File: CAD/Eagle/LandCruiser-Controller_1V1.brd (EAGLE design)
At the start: 98 x 63 mm, 65 parts, among them IC611 LM7805, K311 V23086C1001A403, K312 V23086C1001A403, K313 V23086C1001A403, K314 V23086C1001A403, K315 V23086C1001A403, U101 MEGA8-P, U221 SN75240, U301 MIC2981/2982SO18W, U501 MAX232_SOIC16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

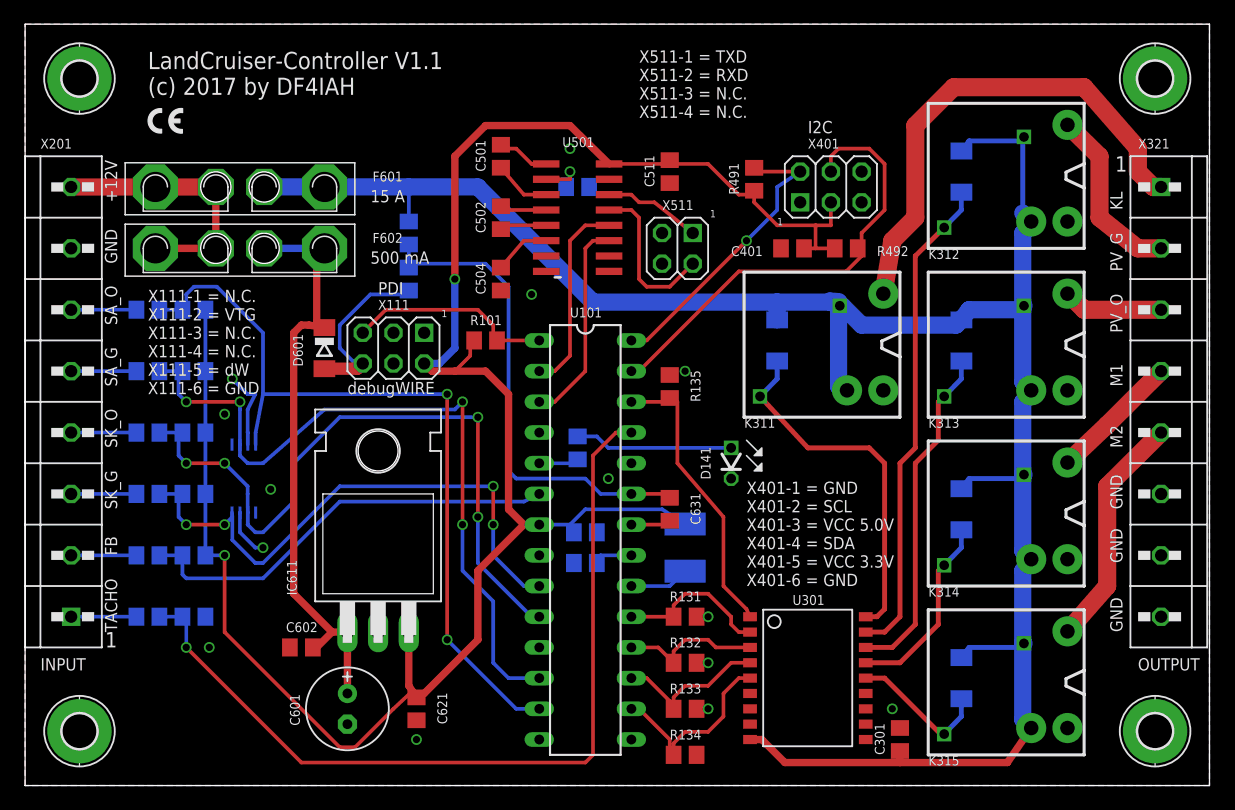
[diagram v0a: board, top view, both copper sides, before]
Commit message: HW_V1.1 - driver switches against ground, not Vbat. Another input line added.
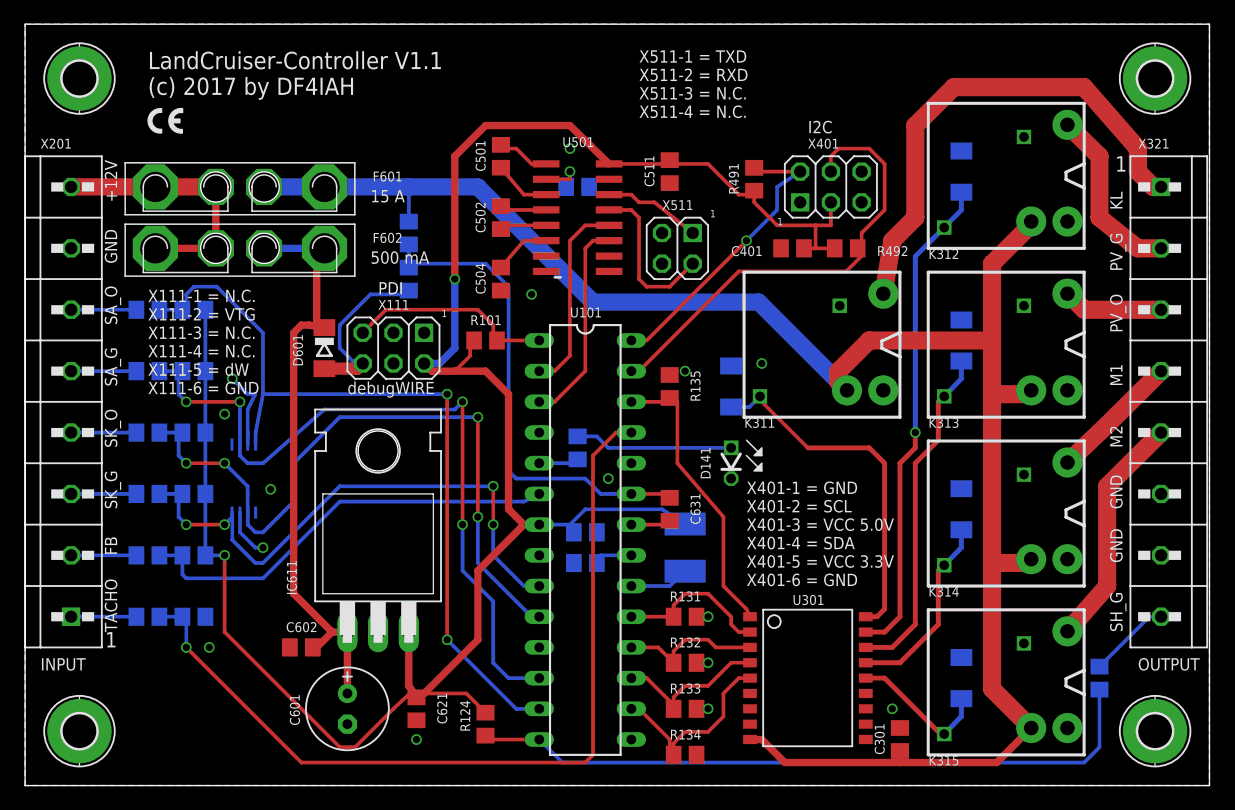
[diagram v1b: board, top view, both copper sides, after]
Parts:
- added R121: 4k7R, rcl:R0805
- added R321: 56R, rcl:R0805
- moved R124 34.1 mm to (38.1, 5.08), flipped to the top, turned to 90 degrees
- moved R122 15.2 mm to (14.0, 34.3)
- moved R123 15.2 mm to (14.0, 39.4), turned to 180 degrees
- moved R125 10.2 mm to (14.0, 24.1), turned to 0 degrees
- moved R126 10.2 mm to (14.0, 29.2), turned to 0 degrees
- moved D311 5.39 mm to (58.4, 33.0), turned to 90 degrees
- turned D312 to 90 degrees
- turned D313 to 90 degrees
- turned D314 to 90 degrees
- turned D315 to 90 degrees
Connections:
- new net MP_SH_G: R124.1, R321.1, U101.14
- new net SH_G: R321.2, X321.8
- net +12V: no longer D311.C, D312.C, D313.C, D314.C, D315.C, K311.1, K312.1, K313.1, K314.1, K315.1
- net +5V: now also R121.2, R123.2, R124.2, R125.1, R126.1; no longer R123.1, R124.1, R125.2, R126.2
- net DRV_KL: now also D311.C; no longer D311.A
- net DRV_M1: now also D314.C; no longer D314.A
- net DRV_M2: now also D315.C; no longer D315.A
- net DRV_PV_G: now also D312.C; no longer D312.A
- net DRV_PV_O: now also D313.C; no longer D313.A
- net GND: now also D311.A, D312.A, D313.A, D314.A, D315.A, K311.1, K312.1, K313.1, K314.1, K315.1; no longer X321.8
- net MP_FB: now also R121.1; no longer R122.1
- net MP_SA_G: now also R122.1; no longer R125.1
- net MP_SA_O: now also R123.1; no longer R126.1
- net MP_SK_G: now also R125.2; no longer R123.2
- net MP_SK_O: now also R126.2; no longer R124.2
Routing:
- net MP_SH_G: track 0.00 -> 57.2 mm
- net +12V: track 175.0 -> 151.2 mm
- net SH_G: track 0.00 -> 6.81 mm
- net +5V: track 173.0 -> 178.8 mm
- net GND: track 28.7 -> 29.5 mm, vias 14 -> 15
- net DRV_KL: track 30.1 -> 29.4 mm
- net DRV_PV_G: vias 0 -> 1
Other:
- board text added: "SH_G"

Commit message: HW_V1.1 - switched FB input with rear tail gate (SH_G)
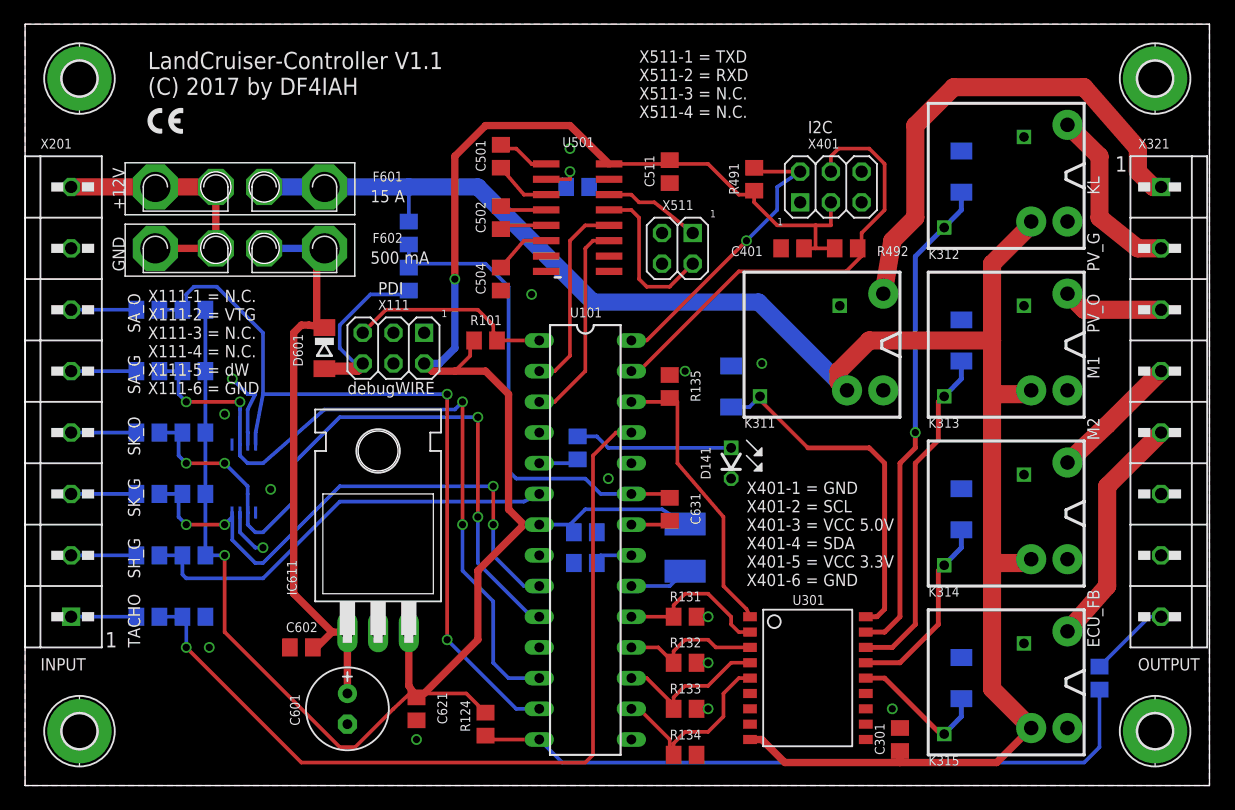
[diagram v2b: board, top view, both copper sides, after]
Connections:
- removed net ECU_FB: R212.1, X201.2
- new net ECU_FB_IN: R321.2, X321.8
- net GND: no longer U301.6, U301.7, U301.8, X321.6, X321.7
- net MP_FB: now also R124.1, R321.1, U101.14; no longer R121.1, R212.2, U101.6
- net MP_SH_G: now also R121.1, R212.2, U101.6; no longer R124.1, R321.1, U101.14
- net SH_G: now also R212.1, X201.2; no longer R321.2, X321.8
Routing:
- net MP_SH_G: track 57.2 -> 35.9 mm
- net MP_FB: track 35.9 -> 56.9 mm
- net ECU_FB_IN: track 0.00 -> 6.81 mm
- net ECU_FB: track 5.40 -> 0.00 mm
- net SH_G: track 6.81 -> 5.40 mm
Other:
- board text added: "ECU_FB"
- board text added: "LandCruiser-Controller V1.1 (C) 2017 by DF4IAH"
- board text removed: "FB"
- board text removed: "LandCruiser-Controller V1.1 (c) 2017 by DF4IAH"
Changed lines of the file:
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@@
 <layers>
 <layer number="1" name="Top" color="4" fill="1" visible="yes" active="yes"/>
-<layer number="2" name="Route2" color="1" fill="3" visible="yes" active="yes"/>
+<layer number="2" name="Route2" color="1" fill="3" visible="no" active="yes"/>
 <layer number="3" name="Route3" color="4" fill="3" visible="no" active="no"/>
 <layer number="4" name="Route4" color="1" fill="4" visible="no" active="no"/>
@@
 <dimension x1="0" y1="62.865" x2="98" y2="62.865" x3="49" y3="70.935" textsize="1.016" layer="47"/>
 <text x="10.16" y="57.15" size="1.4224" layer="21" ratio="15">LandCruiser-Controller V1.1
-(c) 2017 by DF4IAH </text>
+(C) 2017 by DF4IAH </text>
 <text x="64.77" y="53.975" size="1.016" layer="21" ratio="12">I2C</text>
 <polygon width="0.1" layer="21">
@@
 <text x="26.67" y="32.385" size="1.016" layer="21" ratio="12">debugWIRE</text>
 <text x="1.27" y="9.525" size="1.016" layer="21" ratio="12">INPUT</text>
-<text x="7.62" y="48.26" size="1.016" layer="21" ratio="12" rot="R90">+12V</text>
-<text x="7.62" y="43.18" size="1.016" layer="21" ratio="12" rot="R90">GND</text>
+<text x="8.255" y="47.625" size="1.016" layer="21" ratio="12" rot="R90">+12V</text>
+<text x="8.255" y="42.545" size="1.016" layer="21" ratio="12" rot="R90">GND</text>
 <text x="28.575" y="48.26" size="1.016" layer="21" ratio="12">15 A</text>
 <text x="28.575" y="43.18" size="1.016" layer="21" ratio="12">500 mA</text>
-<text x="7.62" y="12.7" size="1.016" layer="21" ratio="12" rot="R90">TACHO</text>
-<text x="7.62" y="19.05" size="1.016" layer="21" ratio="12" rot="R90">FB</text>
-<text x="7.62" y="22.86" size="1.016" layer="21" ratio="12" rot="R90">SK_G</text>
-<text x="7.62" y="27.94" size="1.016" layer="21" ratio="12" rot="R90">SK_O</text>
-<text x="7.62" y="33.02" size="1.016" layer="21" ratio="12" rot="R90">SA_G</text>
-<text x="7.62" y="38.1" size="1.016" layer="21" ratio="12" rot="R90">SA_O</text>
+<text x="9.525" y="11.43" size="1.016" layer="21" ratio="12" rot="R90">TACHO</text>
+<text x="9.525" y="17.145" size="1.016" layer="21" ratio="12" rot="R90">SH_G</text>
+<text x="9.525" y="22.225" size="1.016" layer="21" ratio="12" rot="R90">SK_G</text>
+<text x="9.525" y="27.305" size="1.016" layer="21" ratio="12" rot="R90">SK_O</text>
+<text x="9.525" y="32.385" size="1.016" layer="21" ratio="12" rot="R90">SA_G</text>
+<text x="9.525" y="37.465" size="1.016" layer="21" ratio="12" rot="R90">SA_O</text>
 <text x="92.075" y="9.525" size="1.016" layer="21" ratio="12">OUTPUT</text>
 <text x="50.8" y="55.245" size="1.016" layer="21" ratio="12">X511-1 = TXD
@@
 X511-3 = N.C.
 X511-4 = N.C.</text>
-<text x="90.805" y="47.625" size="1.016" layer="21" ratio="12" rot="R90">KL</text>
-<text x="90.805" y="42.545" size="1.016" layer="21" ratio="12" rot="R90">PV_G</text>
-<text x="90.805" y="37.465" size="1.016" layer="21" ratio="12" rot="R90">PV_O</text>
-<text x="90.805" y="33.02" size="1.016" layer="21" ratio="12" rot="R90">M1</text>
-<text x="90.805" y="27.94" size="1.016" layer="21" ratio="12" rot="R90">M2</text>
-<text x="90.805" y="22.86" size="1.016" layer="21" ratio="12" rot="R90">GND</text>
-<text x="90.805" y="18.415" size="1.016" layer="21" ratio="12" rot="R90">GND</text>
-<text x="90.805" y="12.7" size="1.016" layer="21" ratio="12" rot="R90">SH_G</text>
+<text x="88.9" y="48.895" size="1.016" layer="21" ratio="12" rot="R90">KL</text>
+<text x="88.9" y="42.545" size="1.016" layer="21" ratio="12" rot="R90">PV_G</text>
+<text x="88.9" y="37.465" size="1.016" layer="21" ratio="12" rot="R90">PV_O</text>
+<text x="88.9" y="33.655" size="1.016" layer="21" ratio="12" rot="R90">M1</text>
+<text x="88.9" y="28.575" size="1.016" layer="21" ratio="12" rot="R90">M2</text>
+<text x="88.9" y="11.43" size="1.016" layer="21" ratio="12" rot="R90">ECU_FB</text>
 <text x="57.15" y="47.625" size="0.6096" layer="21" ratio="20" rot="R180">1</text>
 <dimension x1="4.5" y1="4.5" x2="4.445" y2="0" x3="-1.878546875" y3="2.25" textsize="0.8128" layer="47" dtype="vertical"/>
@@
 <contactref element="IC611" pad="2"/>
 <contactref element="U301" pad="10"/>
-<contactref element="U301" pad="6"/>
-<contactref element="U301" pad="7"/>
-<contactref element="U301" pad="8"/>
 <contactref element="K314" pad="3"/>
 <contactref element="K315" pad="3"/>
-<contactref element="X321" pad="7"/>
-<contactref element="X321" pad="6"/>
 <contactref element="U501" pad="15"/>
 <contactref element="C504" pad="2"/>
@@
 </signal>
 <signal name="MP_FB">
-<contactref element="U101" pad="6"/>
-<contactref element="R212" pad="2"/>
-<contactref element="R121" pad="1"/>
-<wire x1="11.11" y1="19.05" x2="13.02" y2="19.05" width="0.3048" layer="16"/>
-<wire x1="13.02" y1="19.05" x2="13.02" y2="17.46" width="0.3048" layer="16"/>
-<wire x1="13.02" y1="17.46" x2="13.335" y2="17.145" width="0.3048" layer="16"/>
-<wire x1="13.335" y1="17.145" x2="19.685" y2="17.145" width="0.3048" layer="16"/>
-<wire x1="19.685" y1="17.145" x2="26.035" y2="23.495" width="0.3048" layer="16"/>
-<wire x1="26.035" y1="23.495" x2="41.275" y2="23.495" width="0.3048" layer="16"/>
-<wire x1="41.275" y1="23.495" x2="42.545" y2="24.13" width="0.3048" layer="16"/>
+<contactref element="R321" pad="1"/>
+<contactref element="U101" pad="14"/>
+<wire x1="42.545" y1="3.81" x2="38.1" y2="3.81" width="0.3048" layer="1"/>
+<wire x1="42.545" y1="3.81" x2="44.45" y2="1.905" width="0.3048" layer="16"/>
+<wire x1="44.45" y1="1.905" x2="87.63" y2="1.905" width="0.3048" layer="16"/>
+<wire x1="87.63" y1="1.905" x2="88.9" y2="3.175" width="0.3048" layer="16"/>
+<contactref element="R124" pad="1"/>
+<wire x1="88.9" y1="3.175" x2="88.9" y2="7.94" width="0.3048" layer="16"/>
+<wire x1="38.1" y1="4.13" x2="38.1" y2="3.81" width="0" layer="19" extent="1-1"/>
 </signal>
 <signal name="MP_SK_O">
@@
 <wire x1="69.85" y1="36.83" x2="80.01" y2="36.83" width="1.5" layer="1"/>
 </signal>
-<signal name="ECU_FB">
+<signal name="SH_G">
 <contactref element="R212" pad="1"/>
 <contactref element="X201" pad="2"/>
@@
 </signal>
 <signal name="MP_SH_G">
-<contactref element="R124" pad="1"/>
-<contactref element="U101" pad="14"/>
-<wire x1="42.545" y1="3.81" x2="38.1" y2="3.81" width="0.3048" layer="1"/>
-<wire x1="38.1" y1="3.81" x2="38.1" y2="4.13" width="0.3048" layer="1"/>
-<wire x1="42.545" y1="3.81" x2="44.45" y2="1.905" width="0.3048" layer="16"/>
-<wire x1="44.45" y1="1.905" x2="87.63" y2="1.905" width="0.3048" layer="16"/>
-<contactref element="R321" pad="1"/>
-<wire x1="87.63" y1="1.905" x2="88.9" y2="3.175" width="0.3048" layer="16"/>
-<wire x1="88.9" y1="3.175" x2="88.9" y2="7.94" width="0.3048" layer="16"/>
-</signal>
-<signal name="SH_G">
+<contactref element="R212" pad="2"/>
+<contactref element="U101" pad="6"/>
+<wire x1="13.02" y1="17.46" x2="13.335" y2="17.145" width="0.3048" layer="16"/>
+<wire x1="13.335" y1="17.145" x2="19.685" y2="17.145" width="0.3048" layer="16"/>
+<wire x1="19.685" y1="17.145" x2="26.035" y2="23.495" width="0.3048" layer="16"/>
+<wire x1="26.035" y1="23.495" x2="41.275" y2="23.495" width="0.3048" layer="16"/>
+<wire x1="41.275" y1="23.495" x2="42.545" y2="24.13" width="0.3048" layer="16"/>
+<contactref element="R121" pad="1"/>
+<wire x1="13.02" y1="17.46" x2="13.02" y2="19.05" width="0.3048" layer="16"/>
+<wire x1="13.02" y1="19.05" x2="11.11" y2="19.05" width="0.3048" layer="16"/>
+</signal>
+<signal name="ECU_FB_IN">
 <contactref element="R321" pad="2"/>
 <contactref element="X321" pad="8"/>
